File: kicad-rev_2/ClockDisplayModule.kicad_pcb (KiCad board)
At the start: 2 copper layers, 88.9 x 20.3 mm, 26 parts, among them IC1 ATMEGA88PA-A, P101 CONN_02X03, P102 CONN_01X05, P203 CONN_01X06, P204 CONN_01X07, Q201 BC856BS, Q202 BC856BS, Q203 BC856BS, U201 SN74LS138, U202 74HC4511

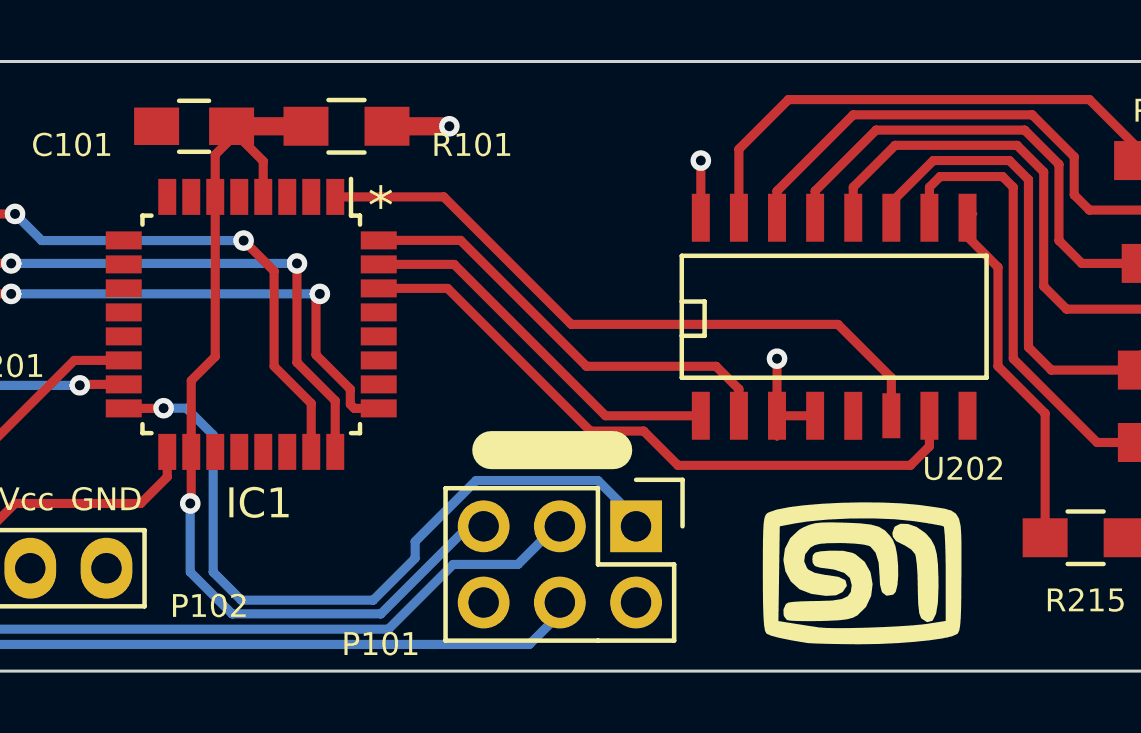
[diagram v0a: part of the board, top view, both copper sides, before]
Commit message: Corrections to the layout based on testing
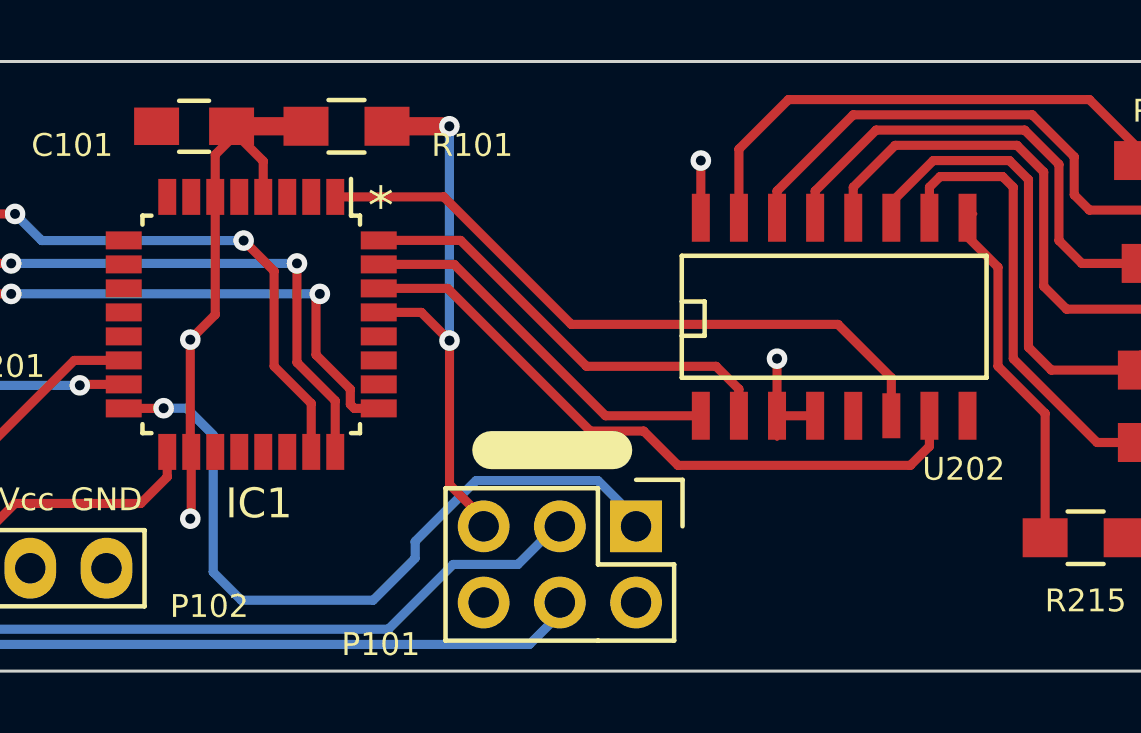
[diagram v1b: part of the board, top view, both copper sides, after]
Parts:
- removed G***: LOGO, ClockFootprints:myLogo_basic_rounded_50
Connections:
- C101 pad 1: Reset -> VCC
- IC1 pad 18: Reset -> VCC
- IC1 pad 29: (no net) -> Reset
- IC1 pad 4: Reset -> VCC
- IC1 pad 6: Reset -> VCC
- R101 pad 1: Reset -> VCC
- R101 pad 2: VCC -> Reset
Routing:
- net VCC: track 11.7 -> 28.6 mm, vias 5 -> 6
- net Reset: track 32.3 -> 18.9 mm, vias 1 -> 2
